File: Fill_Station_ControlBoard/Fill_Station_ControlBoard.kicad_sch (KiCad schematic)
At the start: 34 parts, among them SW1 CK_KMS2xxG, SW2 BOOT, U1 STM32H747IITx, Y1 Crystal 25MHz, Y2 Crystal 32.768 kHz

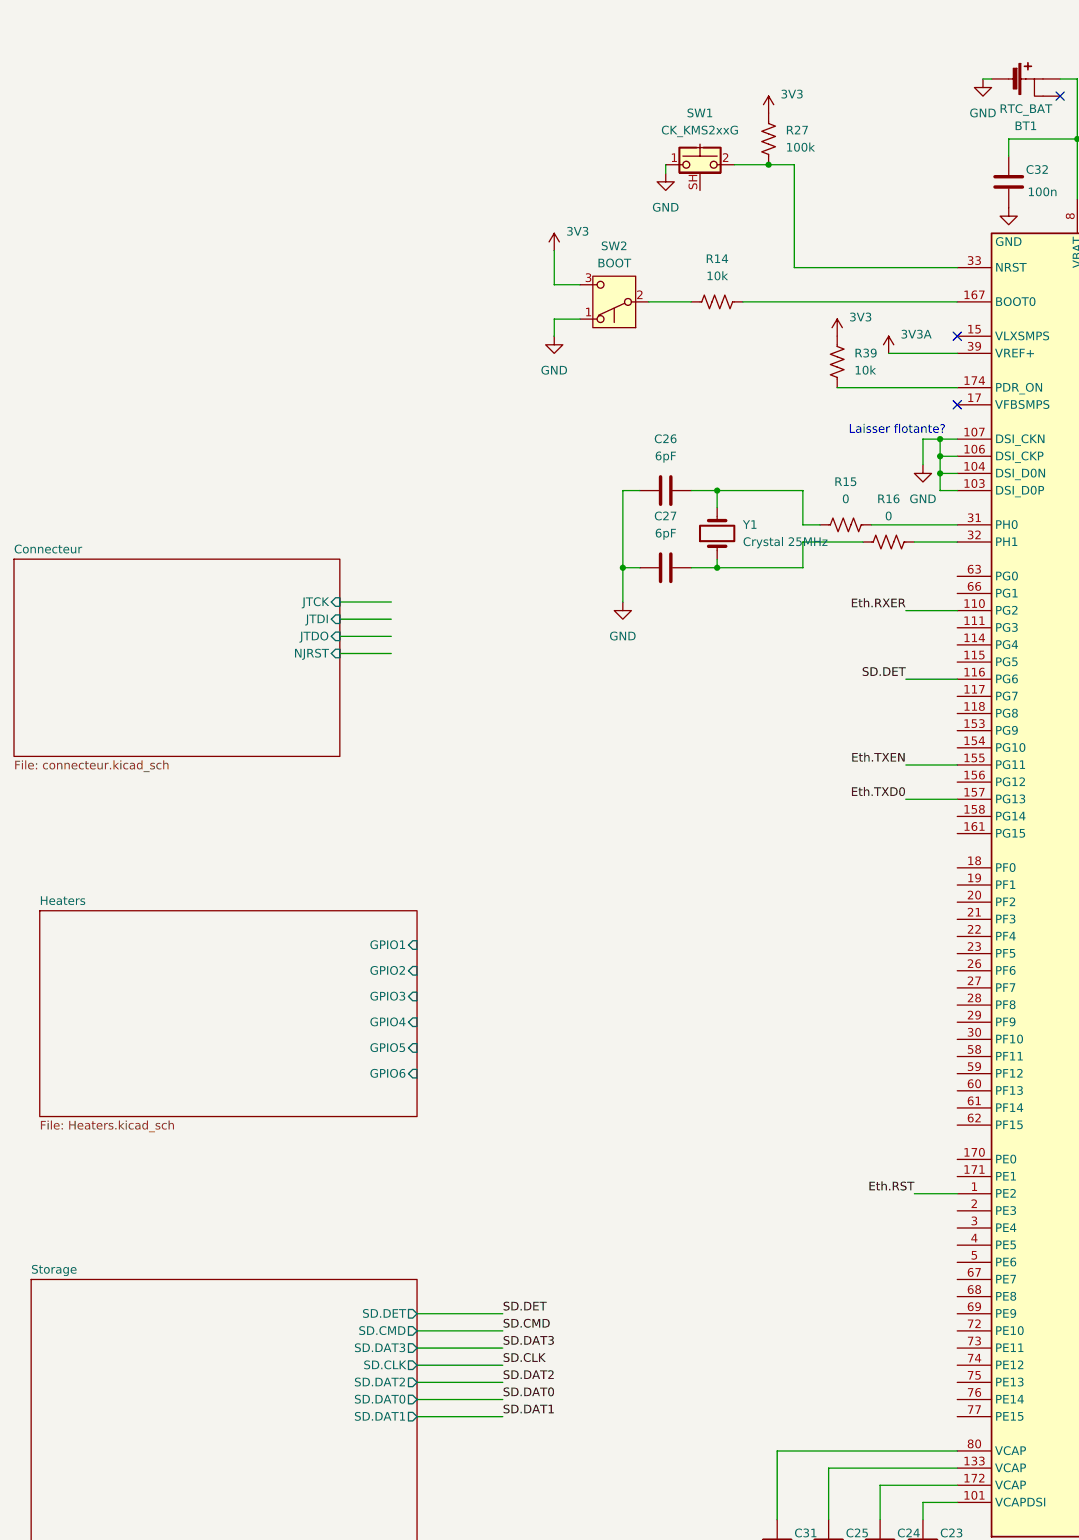
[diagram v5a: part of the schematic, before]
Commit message: Assignation footprint pis valeurs resistances del
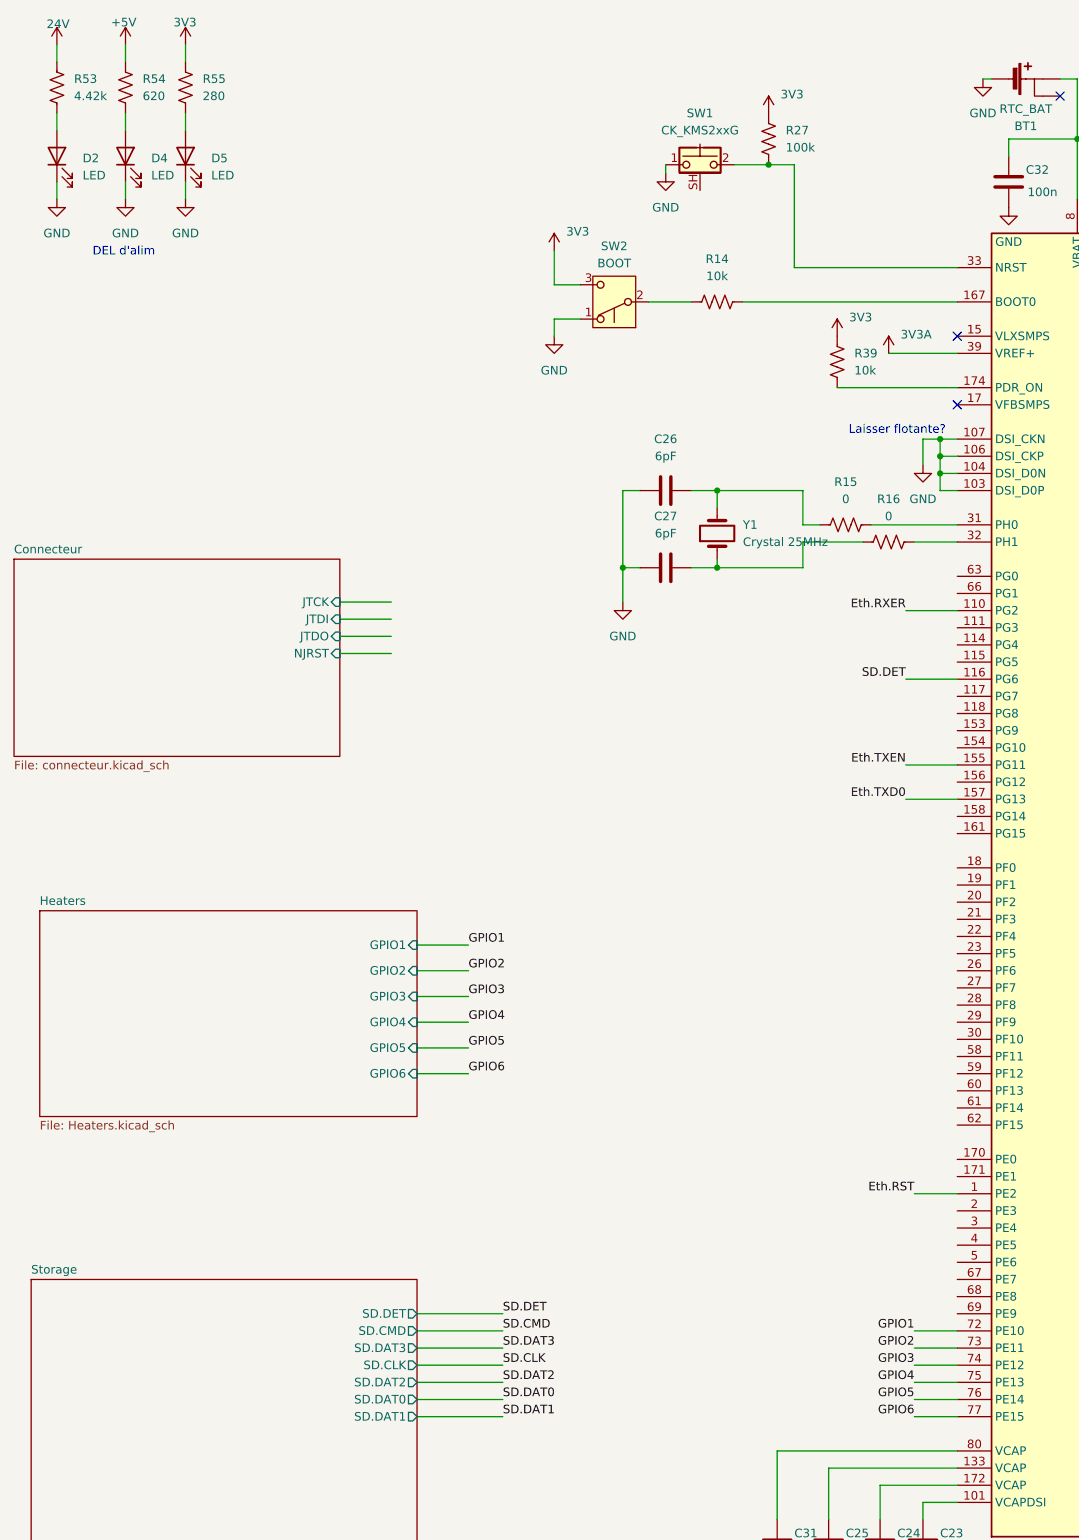
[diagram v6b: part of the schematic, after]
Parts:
- added D2, D4, D5: LED, LED_SMD:LED_0603_1608Metric, symbol Device:LED
- added R53: 4.42k, Resistor_SMD:R_0805_2012Metric, symbol Device:R_US
- added R54: 620, Resistor_SMD:R_0603_1608Metric_Pad0.98x0.95mm_HandSolder, symbol Device:R_US
- added R55: 280, Resistor_SMD:R_0603_1608Metric_Pad0.98x0.95mm_HandSolder, symbol Device:R_US
- C1, C14, C15, C16, C17, C18, C19, C2, C20, C23, C24, C25, C26, C27, C3, C31, C32, C33, C34, C4, C5, C8: footprint (none) -> Capacitor_SMD:C_0603_1608Metric
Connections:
- net 3V3: now also R55.2
- net GND: now also D2.1 (K), D4.1 (K), D5.1 (K)
- net GPIO1: now reaches U1.72 (PE10)
- net GPIO2: now reaches U1.73 (PE11)
- net GPIO3: now reaches U1.74 (PE12)
- net GPIO4: now reaches U1.75 (PE13)
- net GPIO5: now reaches U1.76 (PE14)
- net GPIO6: now reaches U1.77 (PE15)
- new net: D5.2 (A), R55.1
- new net: D4.2 (A), R54.1
- new net: D2.2 (A), R53.1
- new net +5V: R54.2
- new net 24V: R53.2
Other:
- note added: "DEL d'alim"

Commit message: Fait des trucs (commencer arrangement de pièces sur PCB
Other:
- sheet Communication ports: added CAN.FAULT, CAN.RXD, CAN.STBY, CAN.TXD; removed none
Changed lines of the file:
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@@
 	(text "pins ethernet doivent être high impedence lors de la configuaration ou reset du phy"
 		(exclude_from_sim no)
-		(at 373.888 183.642 0)
+		(at 373.634 169.926 0)
 		(effects
 			(font
@@
 	(wire
 		(pts
+			(xy 350.52 175.26) (xy 355.6 175.26)
+		)
+		(stroke
+			(width 0)
+			(type default)
+		)
+	)
+	(wire
+		(pts
 			(xy 161.29 81.28) (xy 163.83 81.28)
 		)
@@
 	(wire
 		(pts
+			(xy 350.52 182.88) (xy 355.6 182.88)
+		)
+		(stroke
+			(width 0)
+			(type default)
+		)
+	)
+	(wire
+		(pts
 			(xy 49.53 40.64) (xy 49.53 43.18)
 		)
@@
 	(wire
 		(pts
+			(xy 350.52 180.34) (xy 355.6 180.34)
+		)
+		(stroke
+			(width 0)
+			(type default)
+		)
+	)
+	(wire
+		(pts
 			(xy 158.75 246.38) (xy 158.75 248.92)
 		)
@@
 	(wire
 		(pts
+			(xy 350.52 177.8) (xy 355.6 177.8)
+		)
+		(stroke
+			(width 0)
+			(type default)
+		)
+	)
+	(wire
+		(pts
 			(xy 157.48 190.5) (xy 163.83 190.5)
 		)
@@
 		)
 	)
+	(label "CAN.STBY"
+		(at 350.52 182.88 180)
+		(effects
+			(font
+				(size 1.27 1.27)
+			)
+			(justify right bottom)
+		)
+	)
+	(label "NJRST"
+		(at 80.01 110.49 0)
+		(effects
+			(font
+				(size 1.27 1.27)
+			)
+			(justify left bottom)
+		)
+	)
 	(label "Eth.RST"
 		(at 350.52 191.77 180)
@@
 		)
 	)
+	(label "CAN.TXD"
+		(at 350.52 180.34 180)
+		(effects
+			(font
+				(size 1.27 1.27)
+			)
+			(justify right bottom)
+		)
+	)
 	(label "GPIO1"
 		(at 157.48 210.82 180)
@@
 		)
 	)
+	(label "CAN.RXD"
+		(at 350.52 177.8 180)
+		(effects
+			(font
+				(size 1.27 1.27)
+			)
+			(justify right bottom)
+		)
+	)
 	(label "Eth.RXER"
 		(at 350.52 210.82 180)
@@
 		)
 	)
+	(label "JTDO"
+		(at 80.01 107.95 0)
+		(effects
+			(font
+				(size 1.27 1.27)
+			)
+			(justify left bottom)
+		)
+	)
 	(label "SD.CLK"
 		(at 96.52 215.9 0)
@@
 		)
 	)
+	(label "CAN.FAULT"
+		(at 350.52 175.26 180)
+		(effects
+			(font
+				(size 1.27 1.27)
+			)
+			(justify right bottom)
+		)
+	)
 	(label "Eth.CRS_DV"
 		(at 267.97 71.12 0)
@@
 		)
 	)
+	(label "JTDI"
+		(at 80.01 105.41 0)
+		(effects
+			(font
+				(size 1.27 1.27)
+			)
+			(justify left bottom)
+		)
+	)
 	(label "Eth.MDC"
 		(at 267.97 142.24 0)
@@
 		)
 	)
+	(label "JTCK"
+		(at 80.01 102.87 0)
+		(effects
+			(font
+				(size 1.27 1.27)
+			)
+			(justify left bottom)
+		)
+	)
 	(label "GPIO4"
 		(at 91.44 165.1 0)
@@
 	)
 	(sheet
-		(at 355.6 189.23)
-		(size 41.91 41.91)
+		(at 355.6 172.72)
+		(size 41.91 58.42)
 		(exclude_from_sim no)
 		(in_bom yes)
@@
 		)
 		(property "Sheetname" "Communication"
-			(at 355.6 188.5184 0)
+			(at 355.6 172.0084 0)
 			(effects
 				(font
@@
 			(effects
 				(font
+					(size 1.27 1.27)
+				)
+				(justify left)
+			)
+		)
+		(pin "CAN.FAULT" output
+			(at 355.6 175.26 180)
+			(effects
+				(font
+					(size 1.27 1.27)
+				)
+				(justify left)
+			)
+		)
+		(pin "CAN.RXD" bidirectional
+			(at 355.6 177.8 180)
+			(effects
+				(font
+					(size 1.27 1.27)
+				)
+				(justify left)
+			)
+		)
+		(pin "CAN.TXD" bidirectional
+			(at 355.6 180.34 180)
+			(effects
+				(font
+					(size 1.27 1.27)
+				)
+				(justify left)
+			)
+		)
+		(pin "CAN.STBY" input
+			(at 355.6 182.88 180)
+			(effects
+				(font

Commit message: arthur
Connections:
- no-connect marks 5 -> 82
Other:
- sheet Connecteur ports: added JTMS; removed none
- sheet Control ports: added Servo.Signal1_1, Servo.Signal1_2, Servo.Signal1_ex, Servo.Signal2_1, Servo.Signal2_2, Servo.Signal2_ex; removed Servo.Signal1, Servo.Signal2
